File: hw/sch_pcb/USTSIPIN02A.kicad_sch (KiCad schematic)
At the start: 63 parts, among them M1 HOLE, M2 HOLE, M3 HOLE, M4 HOLE, M8 BMI-S-204-F, Q1 2SK2394-6, U1 OPA2314, U2 OPA2314, U3 ISL21080DIH312Z-TK 1V25, U4 TS7211, U5 TS5A4594

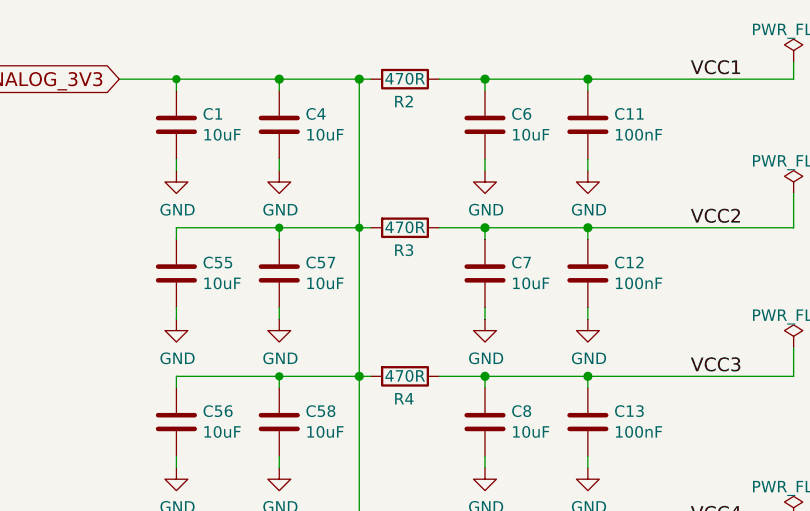
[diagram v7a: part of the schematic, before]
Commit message: uprava hodnot soucastek #1
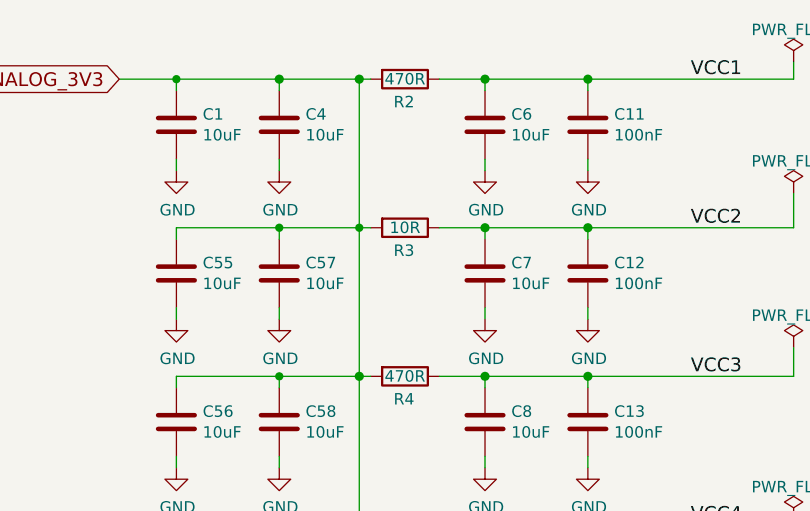
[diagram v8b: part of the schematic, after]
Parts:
- R3: value 470R -> 10R; UST_ID 5c70984512875079b91f8959 -> 5c70984512875079b91f894f
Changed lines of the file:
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@@
     (pin "4")
     (pin "8")
+  )
+  (symbol (lib_id "MLAB_IO:AD8692") (at 156.21 128.27 0) (mirror x) (unit 1)
+    (in_bom yes) (on_board yes)
+    (property "Reference" "U2" (id 0) (at 161.29 125.73 0)
+      (effects (font (size 1.778 1.778)) (justify left))
+    )
+    (property "Value" "OPA2314" (id 1) (at 158.75 121.92 0)
+      (effects (font (size 1.778 1.778)) (justify left))
+    )
+    (property "Footprint" "Package_SO:SOIC-8_3.9x4.9mm_P1.27mm" (id 2) (at 156.21 128.27 0)
+      (effects (font (size 1.524 1.524)) hide)
+    )
+    (property "Datasheet" "" (id 3) (at 169.9514 125.1966 0)
+      (effects (font (size 1.524 1.524)) (justify left))
+    )
+    (property "UST_ID" "5c70984412875079b91f879b" (id 4) (at 156.21 128.27 0)
+      (effects (font (size 1.27 1.27)) hide)
+    )
+    (pin "1")
+    (pin "2")
+    (pin "3")
+    (pin "4")
+    (pin "8")
+  )
+  (symbol (lib_id "MLAB_IO:AD8692") (at 107.95 125.73 0) (unit 2)
+    (in_bom yes) (on_board yes)
+    (property "Reference" "U1" (id 0) (at 110.49 128.27 0)
+      (effects (font (size 1.778 1.778)) (justify left))
+    )
+    (property "Value" "OPA2314" (id 1) (at 107.95 130.81 0)
+      (effects (font (size 1.778 1.778)) (justify left))
+    )
+    (property "Footprint" "Package_SO:SOIC-8_3.9x4.9mm_P1.27mm" (id 2) (at 107.95 125.73 0)
+      (effects (font (size 1.524 1.524)) hide)
+    )
+    (property "Datasheet" "" (id 3) (at 121.6914 128.8034 0)
+      (effects (font (size 1.524 1.524)) (justify left))
+    )
+    (property "UST_ID" "5c70984412875079b91f879b" (id 4) (at 107.95 125.73 0)
+      (effects (font (size 1.27 1.27)) hide)
+    )
     (pin "4")
     (pin "5")
@@
     (pin "8")
   )
-  (symbol (lib_id "MLAB_IO:AD8692") (at 156.21 128.27 0) (mirror x) (unit 1)
-    (in_bom yes) (on_board yes)
-    (property "Reference" "U2" (id 0) (at 161.29 125.73 0)
+  (symbol (lib_id "MLAB_IO:AD8692") (at 229.87 96.52 0) (unit 2)
+    (in_bom yes) (on_board yes)
+    (property "Reference" "U2" (id 0) (at 232.41 100.33 0)
       (effects (font (size 1.778 1.778)) (justify left))
     )
-    (property "Value" "OPA2314" (id 1) (at 158.75 121.92 0)
+    (property "Value" "OPA2314" (id 1) (at 229.87 102.87 0)
       (effects (font (size 1.778 1.778)) (justify left))
     )
-    (property "Footprint" "Package_SO:SOIC-8_3.9x4.9mm_P1.27mm" (id 2) (at 156.21 128.27 0)
+    (property "Footprint" "Package_SO:SOIC-8_3.9x4.9mm_P1.27mm" (id 2) (at 229.87 96.52 0)
       (effects (font (size 1.524 1.524)) hide)
     )
-    (property "Datasheet" "" (id 3) (at 169.9514 125.1966 0)
+    (property "Datasheet" "" (id 3) (at 243.6114 99.5934 0)
       (effects (font (size 1.524 1.524)) (justify left))
     )
-    (property "UST_ID" "5c70984412875079b91f879b" (id 4) (at 156.21 128.27 0)
-      (effects (font (size 1.27 1.27)) hide)
-    )
-    (pin "1")
-    (pin "2")
-    (pin "3")
-    (pin "4")
-    (pin "8")
+    (property "UST_ID" "5c70984412875079b91f879b" (id 4) (at 229.87 96.52 0)
+      (effects (font (size 1.27 1.27)) hide)
+    )
     (pin "4")
     (pin "5")
@@
     (pin "8")
   )
-  (symbol (lib_id "MLAB_IO:AD8692") (at 107.95 125.73 0) (unit 2)
-    (in_bom yes) (on_board yes)
-    (property "Reference" "U1" (id 0) (at 110.49 128.27 0)
-      (effects (font (size 1.778 1.778)) (justify left))
-    )
-    (property "Value" "OPA2314" (id 1) (at 107.95 130.81 0)
-      (effects (font (size 1.778 1.778)) (justify left))
-    )
-    (property "Footprint" "Package_SO:SOIC-8_3.9x4.9mm_P1.27mm" (id 2) (at 107.95 125.73 0)
-      (effects (font (size 1.524 1.524)) hide)
-    )
-    (property "Datasheet" "" (id 3) (at 121.6914 128.8034 0)
-      (effects (font (size 1.524 1.524)) (justify left))
-    )
-    (property "UST_ID" "5c70984412875079b91f879b" (id 4) (at 107.95 125.73 0)
-      (effects (font (size 1.27 1.27)) hide)
-    )
-    (pin "1")
-    (pin "2")
-    (pin "3")
-    (pin "4")
-    (pin "8")
-    (pin "4")
-    (pin "5")
-    (pin "6")
-    (pin "7")
-    (pin "8")
-  )
-  (symbol (lib_id "MLAB_IO:AD8692") (at 229.87 96.52 0) (unit 2)
-    (in_bom yes) (on_board yes)
-    (property "Reference" "U2" (id 0) (at 232.41 100.33 0)
-      (effects (font (size 1.778 1.778)) (justify left))
-    )
-    (property "Value" "OPA2314" (id 1) (at 229.87 102.87 0)
-      (effects (font (size 1.778 1.778)) (justify left))
-    )
-    (property "Footprint" "Package_SO:SOIC-8_3.9x4.9mm_P1.27mm" (id 2) (at 229.87 96.52 0)
-      (effects (font (size 1.524 1.524)) hide)
-    )
-    (property "Datasheet" "" (id 3) (at 243.6114 99.5934 0)
-      (effects (font (size 1.524 1.524)) (justify left))
-    )
-    (property "UST_ID" "5c70984412875079b91f879b" (id 4) (at 229.87 96.52 0)
-      (effects (font (size 1.27 1.27)) hide)
-    )
-    (pin "1")
-    (pin "2")
-    (pin "3")
-    (pin "4")
-    (pin "8")
-    (pin "4")
-    (pin "5")
-    (pin "6")
-    (pin "7")
-    (pin "8")
-  )
   (symbol (lib_id "Device:C") (at 44.45 132.08 0) (unit 1)
     (in_bom yes) (on_board yes)
@@
       (effects (font (size 1.27 1.27)) (justify left))
     )
-    (property "Value" "470R" (id 1) (at 76.2 36.83 90))
+    (property "Value" "10R" (id 1) (at 76.2 36.83 90))
     (property "Footprint" "Resistor_SMD:R_0603_1608Metric" (id 2) (at 76.2 35.052 90)
       (effects (font (size 1.27 1.27)) hide)
@@
       (effects (font (size 1.27 1.27)) hide)
     )
-    (property "UST_ID" "5c70984512875079b91f8959" (id 4) (at 76.2 36.83 0)
+    (property "UST_ID" "5c70984512875079b91f894f" (id 4) (at 76.2 36.83 0)
       (effects (font (size 1.27 1.27)) hide)
     )
@@
     )
     (path "/00000000-0000-0000-0000-00005b4bb90e"
-      (reference "R3") (unit 1) (value "470R") (footprint "Resistor_SMD:R_0603_1608Metric")
+      (reference "R3") (unit 1) (value "10R") (footprint "Resistor_SMD:R_0603_1608Metric")
     )
     (path "/00000000-0000-0000-0000-00005b4c8409"
@@
     )
     (path "/00000000-0000-0000-0000-00005c4aedd8/ea9b3730-00b4-4c9e-b83b-e46a67ce029b"
-      (reference "R45") (unit 1) (value "100R") (footprint "Resistor_SMD:R_0603_1608Metric")
+      (reference "R45") (unit 1) (value "10R") (footprint "Resistor_SMD:R_0603_1608Metric")
     )
     (path "/00000000-0000-0000-0000-00005b39c1e6"
